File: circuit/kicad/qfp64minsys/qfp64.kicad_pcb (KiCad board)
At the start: 2 copper layers, 80.5 x 33.2 mm, 39 parts, among them J1 USB_B_Mini, J10 Conn_01x03_Pin, J11 Conn_01x09_Pin, J12 Conn_01x12_Pin, J2 USB_B_Mini, J3 Conn_01x03_Pin, J4 Conn_01x05_Pin, J5 Conn_01x09_Pin, J6 Conn_01x09_Pin, J7 Conn_01x03_Pin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

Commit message: Update PCB
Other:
- board text added: "3V3"
- board text added: "5V"
- board text added: "BOOT0"
- board text added: "GND"
- board text added: "SWD"
- board text added: "UART"
- board text added: "USER"
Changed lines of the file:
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@@
       (layerselection 0x00010fc_ffffffff)
       (plot_on_all_layers_selection 0x0000000_00000000)
-      (disableapertmacros false)
+      (disableapertmacros true)
       (usegerberextensions false)
       (usegerberattributes true)
@@
     (property "ki_keywords" "switch normally-open pushbutton push-button")
     (attr through_hole)
-    (fp_text reference "SW1" (at 3.25 -2) (layer "F.SilkS")
+    (fp_text reference "SW1" (at 3.25 -2) (layer "F.SilkS") hide
         (effects (font (size 1 1) (thickness 0.15)))
     )
@@
   (gr_rect (start 115.875 75.55) (end 196.375 108.75)
     (stroke (width 0.1) (type default)) (fill none) (layer "Edge.Cuts"))
+  (gr_text "BOOT0\n" (at 163.2 80.7) (layer "F.SilkS")
+    (effects (font (size 1 1) (thickness 0.25) bold) (justify left bottom))
+  )
+  (gr_text "5V" (at 123.7 104.9) (layer "F.SilkS")
+    (effects (font (size 1 1) (thickness 0.25) bold) (justify left bottom))
+  )
+  (gr_text "3V3" (at 131.4 93.7) (layer "F.SilkS")
+    (effects (font (size 1 1) (thickness 0.25) bold) (justify left bottom))
+  )
+  (gr_text "USER" (at 129.2 89.9) (layer "F.SilkS")
+    (effects (font (size 1 1) (thickness 0.25) bold) (justify left bottom))
+  )
+  (gr_text "SWD" (at 163.3 85.8) (layer "F.SilkS")
+    (effects (font (size 1 1) (thickness 0.25) bold) (justify left bottom))
+  )
+  (gr_text "GND" (at 188.6 95) (layer "F.SilkS")
+    (effects (font (size 1 1) (thickness 0.25) bold) (justify left bottom))
+  )
+  (gr_text "UART\n" (at 162.9 94.9) (layer "F.SilkS")
+    (effects (font (size 1 1) (thickness 0.25) bold) (justify left bottom))
+  )
   (segment (start 174.075 80.55) (end 173.175 81.45) (width 0.5) (layer "F.Cu") (net 1))
   (segment (start 178.945 80.92) (end 178.575 80.55) (width 0.5) (layer "F.Cu") (net 1))

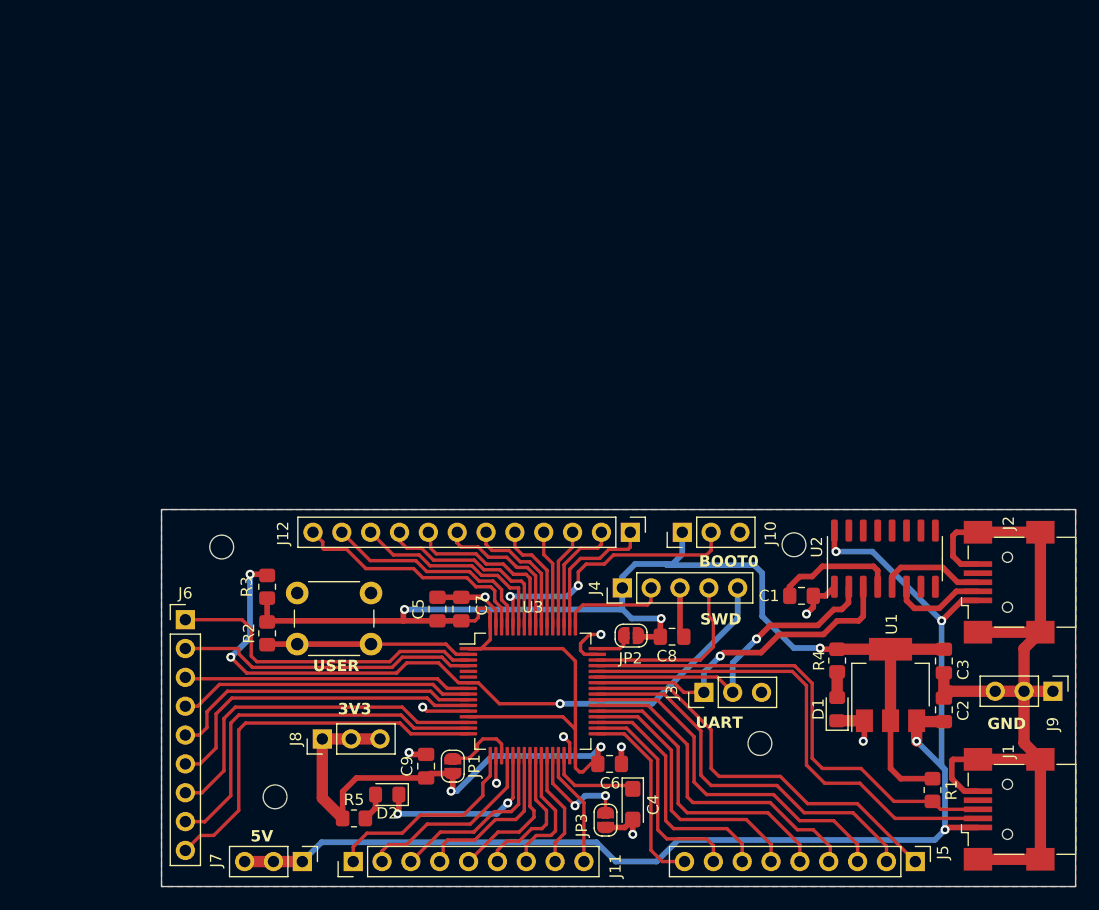
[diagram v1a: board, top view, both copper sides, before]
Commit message: Update PCB LQFP64
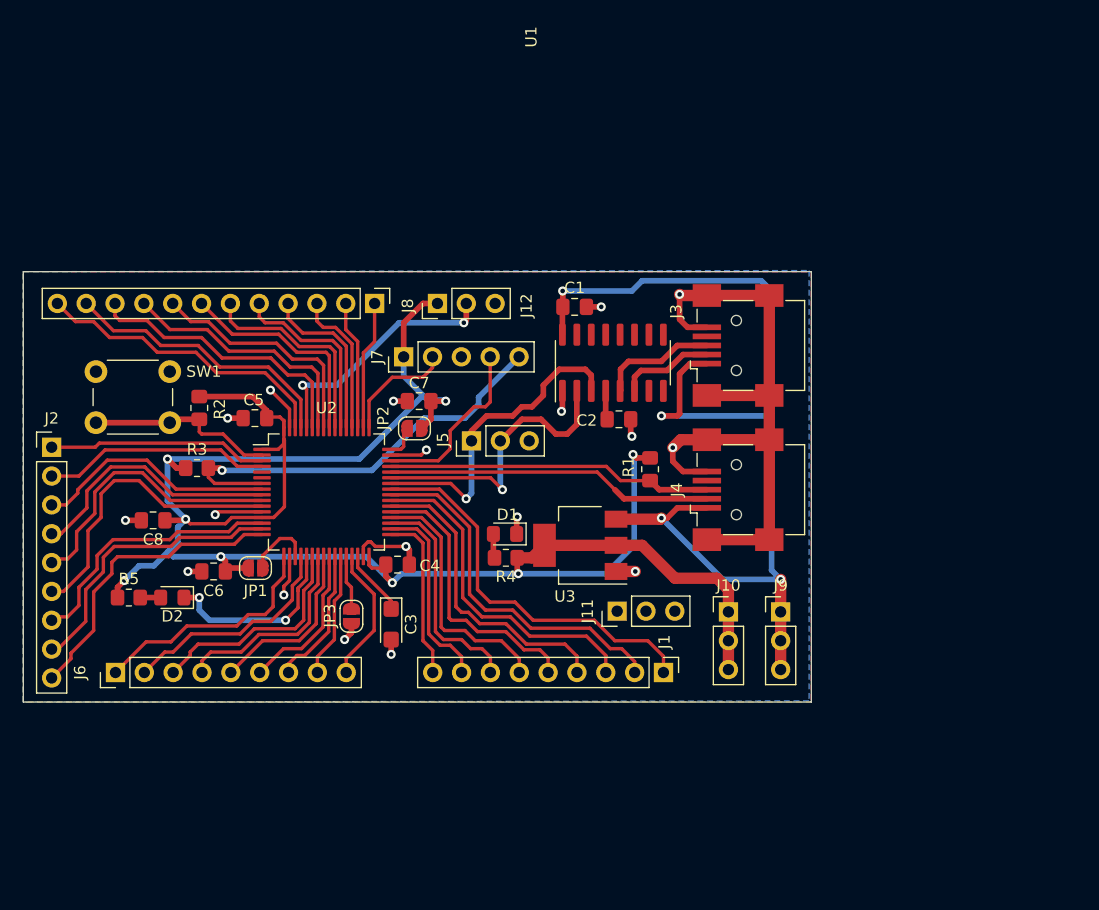
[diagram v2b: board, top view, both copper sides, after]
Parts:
- removed C9: 10nF, Capacitor_SMD:C_0805_2012Metric_Pad1.18x1.45mm_HandSolder
- removed H1, H2, H3, H4: MountingHole, MountingHole:MountingHole_2.1mm
- C3: value 100nF -> 4u7F; footprint Capacitor_SMD:C_0805_2012Metric_Pad1.18x1.45mm_HandSolder -> Capacitor_Tantalum_SMD:CP_EIA-3216-18_Kemet-A
- C4: value 4u7F -> 100nF; footprint Capacitor_Tantalum_SMD:CP_EIA-3216-18_Kemet-A -> Capacitor_SMD:C_0805_2012Metric_Pad1.18x1.45mm_HandSolder
- C6, C7, C8: value 10nF -> 100nF
- J1, J2: value USB_B_Mini -> Conn_01x09_Pin; footprint Connector_USB:USB_Mini-B_Wuerth_65100516121_Horizontal -> Connector_PinHeader_2.54mm:PinHeader_1x09_P2.54mm_Vertical
- J11, J5: value Conn_01x09_Pin -> Conn_01x03_Pin; footprint Connector_PinHeader_2.54mm:PinHeader_1x09_P2.54mm_Vertical -> Connector_PinHeader_2.54mm:PinHeader_1x03_P2.54mm_Vertical
- J12: value Conn_01x12_Pin -> Conn_01x03_Pin; footprint Connector_PinHeader_2.54mm:PinHeader_1x12_P2.54mm_Vertical -> Connector_PinHeader_2.54mm:PinHeader_1x03_P2.54mm_Vertical
- J3: value Conn_01x03_Pin -> USB_B_Mini; footprint Connector_PinHeader_2.54mm:PinHeader_1x03_P2.54mm_Vertical -> Connector_USB:USB_Mini-B_Wuerth_65100516121_Horizontal
- J4: value Conn_01x05_Pin -> USB_B_Mini; footprint Connector_PinHeader_2.54mm:PinHeader_1x05_P2.54mm_Vertical -> Connector_USB:USB_Mini-B_Wuerth_65100516121_Horizontal
- J7: value Conn_01x03_Pin -> Conn_01x05_Pin; footprint Connector_PinHeader_2.54mm:PinHeader_1x03_P2.54mm_Vertical -> Connector_PinHeader_2.54mm:PinHeader_1x05_P2.54mm_Vertical
- J8: value Conn_01x03_Pin -> Conn_01x12_Pin; footprint Connector_PinHeader_2.54mm:PinHeader_1x03_P2.54mm_Vertical -> Connector_PinHeader_2.54mm:PinHeader_1x12_P2.54mm_Vertical
- U1: value AMS1117-3.3 -> CH340C; footprint Package_TO_SOT_SMD:SOT-223-3_TabPin2 -> Package_SO:SOIC-16_3.9x9.9mm_P1.27mm
- U2: value CH340C -> STM32F401RETx; footprint Package_SO:SOIC-16_3.9x9.9mm_P1.27mm -> Package_QFP:LQFP-64_10x10mm_P0.5mm
- U3: value STM32F401RETx -> AMS1117-3.3; footprint Package_QFP:LQFP-64_10x10mm_P0.5mm -> Package_TO_SOT_SMD:SOT-223-3_TabPin2
- moved J2 85.0 mm to (106.2, 70.1), turned to 0 degrees
- moved J5 53.9 mm to (143.2, 69.5), turned to 90 degrees
- moved U2 49.5 mm to (130.4, 74.0), turned to 0 degrees
- moved C3 48.8 mm to (136.1, 85.7)
- moved C8 46.8 mm to (115.1, 76.5), turned to 180 degrees
- moved J7 45.3 mm to (137.2, 62.1), turned to 90 degrees
- moved C6 38.8 mm to (120.5, 81.0), turned to 180 degrees
- moved J8 38.6 mm to (134.6, 57.4), turned to -90 degrees
- moved C2 38.4 mm to (156.2, 67.6), turned to 0 degrees
- moved R1 37.6 mm to (158.9, 72.0)
- moved U1 37.5 mm to (155.6, 62.6)
- moved D1 33.1 mm to (146.1, 77.7), turned to 180 degrees
- moved J1 32.6 mm to (160.1, 89.9), turned to -90 degrees
- moved C1 32.4 mm to (152.3, 57.7)
- moved J11 32.0 mm to (156.0, 84.5)
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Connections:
- C1 pad 1: Net-(U2-V3) -> +5V
- C2 pad 1: +5V -> Net-(U1-V3)
- C3 pad 1: VDD -> VCAP
- C4 pad 1: VCAP -> VDD
- J1 pad 1: +5V -> PA8
- J1 pad 2: USBDM -> PC9
- J1 pad 3: USBDP -> PC8
- J1 pad 4: unconnected-(J1-ID-Pad4) -> PC7
- J1 pad 5: GND -> PC6
- J1 pad 6: GND -> PB15
- J10 pad 2: BOOT0 -> VDD
- J10 pad 3: GND -> VDD
- J11 pad 1: PA3 -> GND
- J11 pad 2: PA4 -> GND
- J11 pad 3: PA6 -> GND
- J12 pad 1: PA15 -> VDD
- J12 pad 2: PC10 -> BOOT0
- J12 pad 3: PC11 -> GND
- J2 pad 1: +5V -> PC14
- J2 pad 2: Net-(J2-D-) -> PC15
- J2 pad 3: Net-(J2-D+) -> PC0
- J2 pad 4: unconnected-(J2-ID-Pad4) -> PC1
- J2 pad 5: GND -> PC2
- J2 pad 6: GND -> PC3
- J3 pad 1: TXD -> +5V
- J3 pad 2: RXD -> Net-(J3-D-)
- J3 pad 3: GND -> Net-(J3-D+)
- J4 pad 1: VDD -> +5V
- J4 pad 2: SWCLK -> USBDM
- J4 pad 3: GND -> USBDP
- J4 pad 4: SWDIO -> unconnected-(J4-ID-Pad4)
- J4 pad 5: NRST -> GND
- J5 pad 1: PA8 -> TXD
- J5 pad 2: PC9 -> RXD
- J5 pad 3: PC8 -> GND
- J6 pad 1: PC14 -> PA3
- J6 pad 2: PC15 -> PA4
- J6 pad 3: PC0 -> PA6
- J6 pad 4: PC1 -> PA7
- J6 pad 5: PC2 -> PC4
- J6 pad 6: PC3 -> PC5
- J6 pad 7: PA0 -> PB0
- J6 pad 8: PA1 -> PB1
- J6 pad 9: PA2 -> PB10
- J7 pad 1: +5V -> VDD
- J7 pad 2: +5V -> SWCLK
- J7 pad 3: +5V -> GND
- J8 pad 1: VDD -> PA15
- J8 pad 2: VDD -> PC10
- J8 pad 3: VDD -> PC11
- J9 pad 1: GND -> +5V
- J9 pad 2: GND -> +5V
- J9 pad 3: GND -> +5V
- U1 pad 2: VDD -> RXD
- U1 pad 3: +5V -> TXD
- U2 pad 1: GND -> VDD
- U2 pad 10: unconnected-(U2-~{DSR}-Pad10) -> PC2
- U2 pad 11: unconnected-(U2-~{RI}-Pad11) -> PC3
- U2 pad 12: unconnected-(U2-~{DCD}-Pad12) -> GND
- U2 pad 13: unconnected-(U2-~{DTR}-Pad13) -> VDD
- U2 pad 14: unconnected-(U2-~{RTS}-Pad14) -> PA0
- U2 pad 15: unconnected-(U2-R232-Pad15) -> PA1
- U2 pad 16: +5V -> PA2
- U2 pad 2: RXD -> BTN
- U2 pad 3: TXD -> PC14
- U2 pad 4: Net-(U2-V3) -> PC15
- U2 pad 5: Net-(J2-D+) -> unconnected-(U2-PH0-Pad5)
- U2 pad 6: Net-(J2-D-) -> unconnected-(U2-PH1-Pad6)
- U2 pad 7: unconnected-(U2-NC-Pad7) -> NRST
- U2 pad 8: unconnected-(U2-NC-Pad8) -> PC0
- U2 pad 9: unconnected-(U2-~{CTS}-Pad9) -> PC1
- U3 pad 1: VDD -> GND
- U3 pad 2: BTN -> VDD
- U3 pad 3: PC14 -> +5V
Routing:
- net NRST: track 62.4 -> 37.7 mm, vias 3 -> 1
- net GND: track 117.6 -> 96.6 mm, vias 10 -> 18
- net +5V: track 111.2 -> 95.6 mm
- net USBDM: track 43.0 -> 28.8 mm
- net USBDP: track 42.6 -> 28.7 mm
- net Net-(U2-V3): track 10.9 -> 0.00 mm
- net Net-(J3-D+): track 0.00 -> 10.4 mm
- net Net-(J2-D+): track 9.35 -> 0.00 mm
- net PC14: track 28.5 -> 19.3 mm
- net Net-(J3-D-): track 0.00 -> 8.42 mm
- net Net-(J2-D-): track 8.41 -> 0.00 mm
- net PA1: track 33.1 -> 25.3 mm
- net PA0: track 31.3 -> 23.7 mm
- net PA2: track 34.1 -> 26.6 mm
- net PB3: track 11.7 -> 18.5 mm
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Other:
- board size 80.5 x 33.2 mm -> 69.4 x 37.9 mm
- board text removed: "3V3"
- board text removed: "5V"
- board text removed: "BOOT0"
- board text removed: "GND"
- board text removed: "SWD"
- board text removed: "UART"
- board text removed: "USER"
